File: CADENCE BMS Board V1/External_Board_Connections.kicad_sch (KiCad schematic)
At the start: 42 parts, among them J10 Conn_01x08, J11 Conn_01x06, J12 Conn_01x02, J13 Conn_01x08, J14 Conn_01x04, J15 Conn_01x08, J2 Conn_01x02, J27 USB_C_Receptacle_USB2.0_16P, J3 Conn_01x08, J4 Conn_01x02, J5 Conn_01x01_Socket, J6 Conn_01x01_Socket, J7 Conn_01x01_Socket, J8 Conn_01x01_Socket, J9 Conn_01x04, Q27 Q_PMOS_DGS, Q28 Q_PMOS_DGS, U11 CYPD3177-24LQ

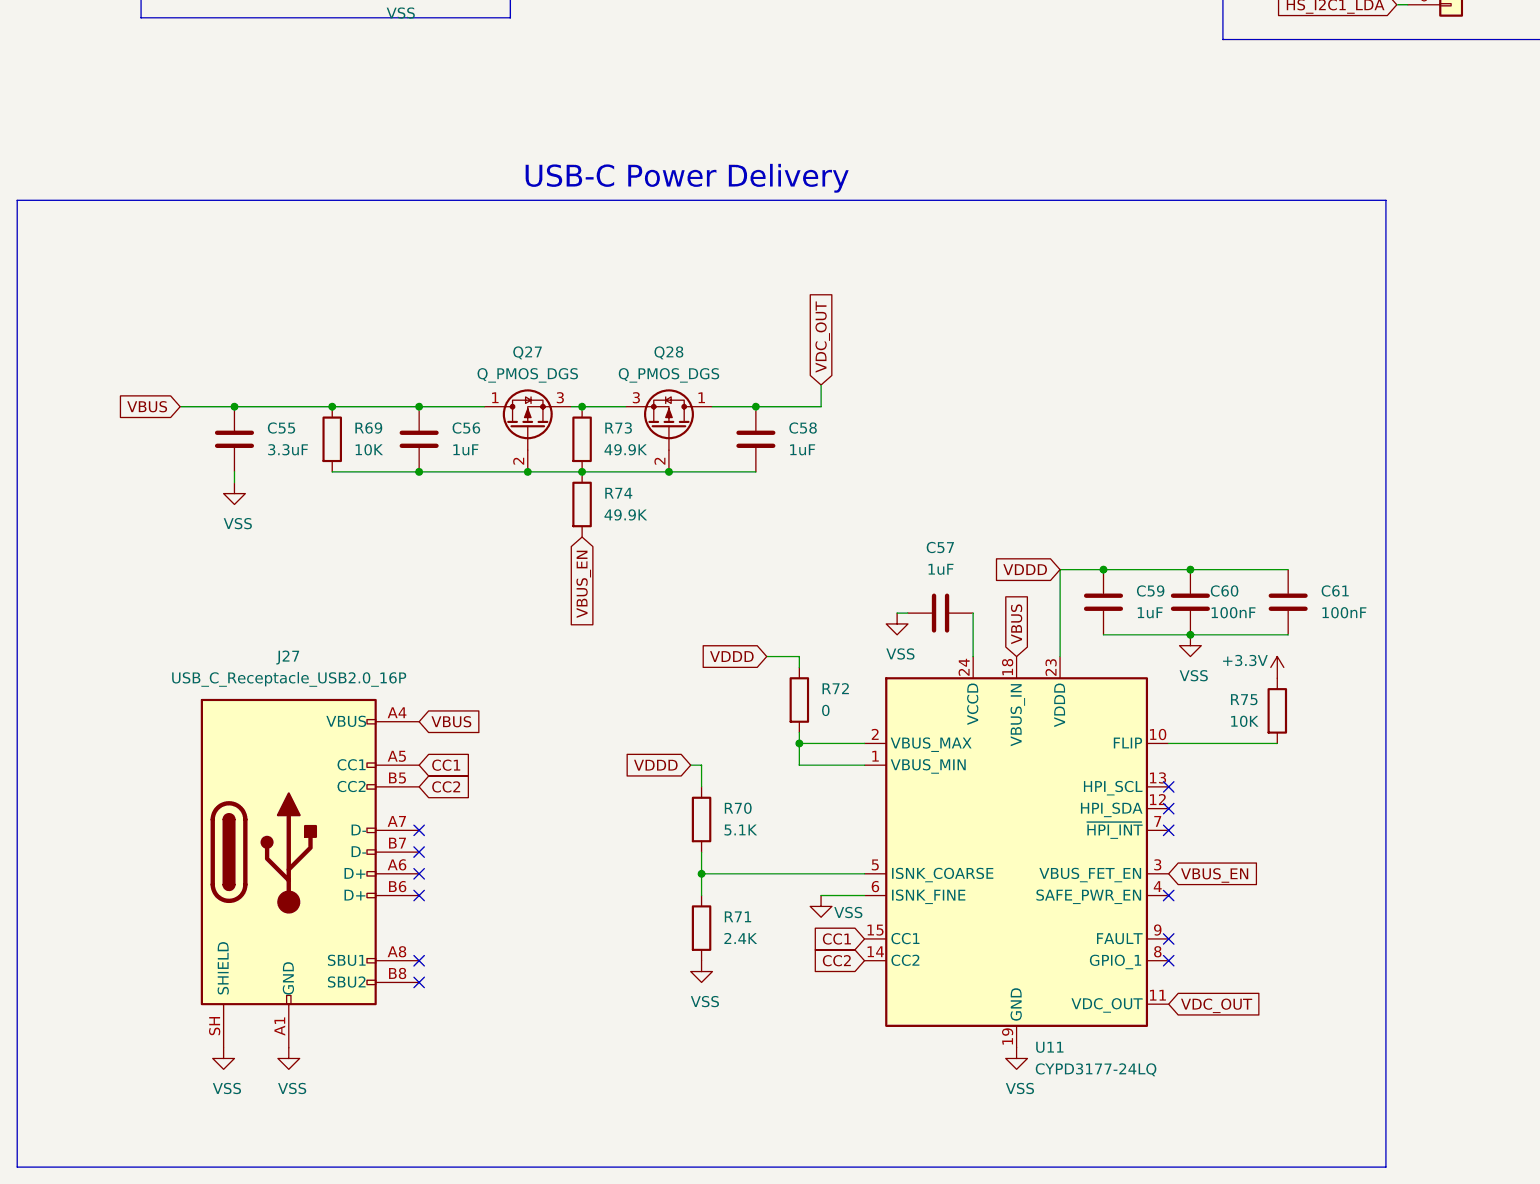
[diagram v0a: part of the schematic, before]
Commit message: Updates for banana plug power testing
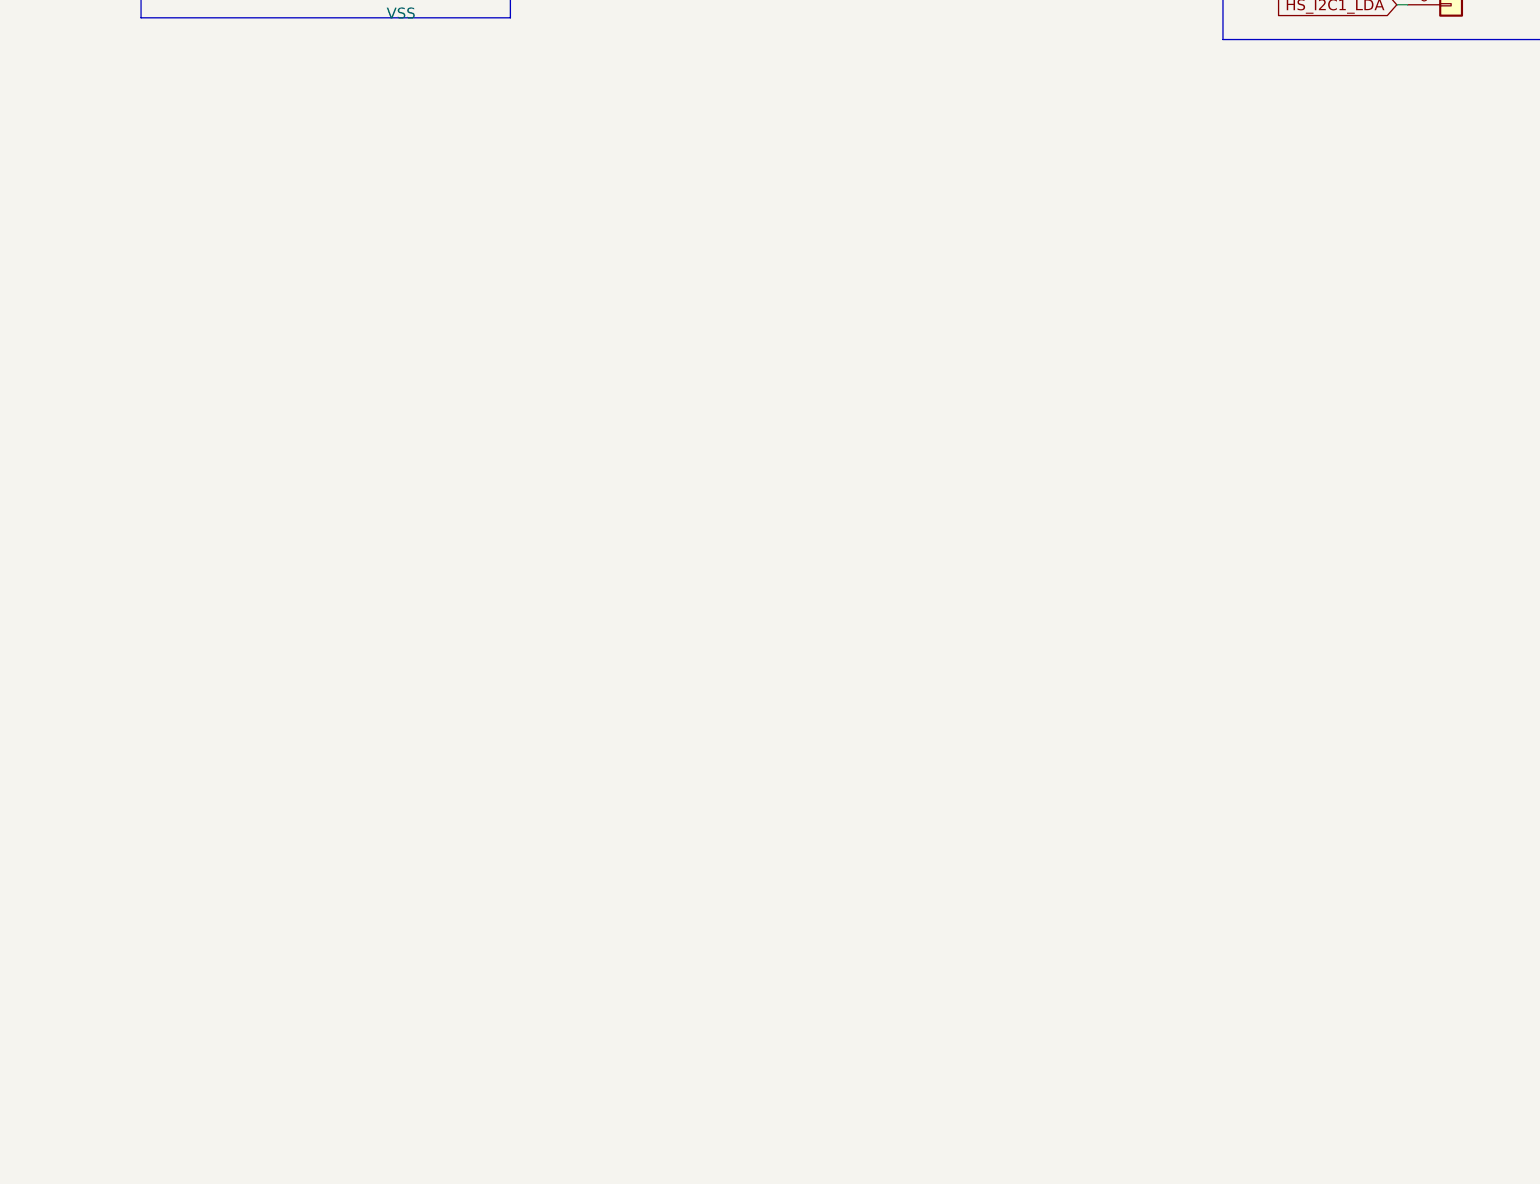
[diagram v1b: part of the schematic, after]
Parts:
- removed C55: 3.3uF, Capacitor_SMD:C_0805_2012Metric, symbol Device:C
- removed C56, C57, C58, C59: 1uF, Capacitor_SMD:C_0805_2012Metric, symbol Device:C
- removed C60, C61: 100nF, Capacitor_SMD:C_0603_1608Metric, symbol Device:C
- removed J27: USB_C_Receptacle_USB2.0_16P, Connector_USB:USB_C_Receptacle_HRO_TYPE-C-31-M-12, symbol Connector:USB_C_Receptacle_USB2.0_16P
- removed Q27, Q28: Q_PMOS_DGS, Package_TO_SOT_SMD:SOT-23, symbol Transistor_FET:Q_PMOS_DGS
- removed R69: 10K, Resistor_SMD:R_0603_1608Metric_Pad0.98x0.95mm_HandSolder, symbol Device:R
- removed R70: 5.1K, Resistor_SMD:R_0603_1608Metric_Pad0.98x0.95mm_HandSolder, symbol Device:R
- removed R71: 2.4K, Resistor_SMD:R_0603_1608Metric, symbol Device:R
- removed R72: 0, Resistor_SMD:R_0603_1608Metric, symbol Device:R
- removed R73, R74: 49.9K, Resistor_SMD:R_0603_1608Metric, symbol Device:R
- removed R75: 10K, Resistor_SMD:R_0603_1608Metric, symbol Device:R
- removed U11: CYPD3177-24LQ, Package_DFN_QFN:QFN-24-1EP_4x4mm_P0.5mm_EP2.75x2.75mm, symbol Interface_USB:CYPD3177-24LQ
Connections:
- no-connect marks 12 -> 0
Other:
- note removed: "USB-C Power Delivery"

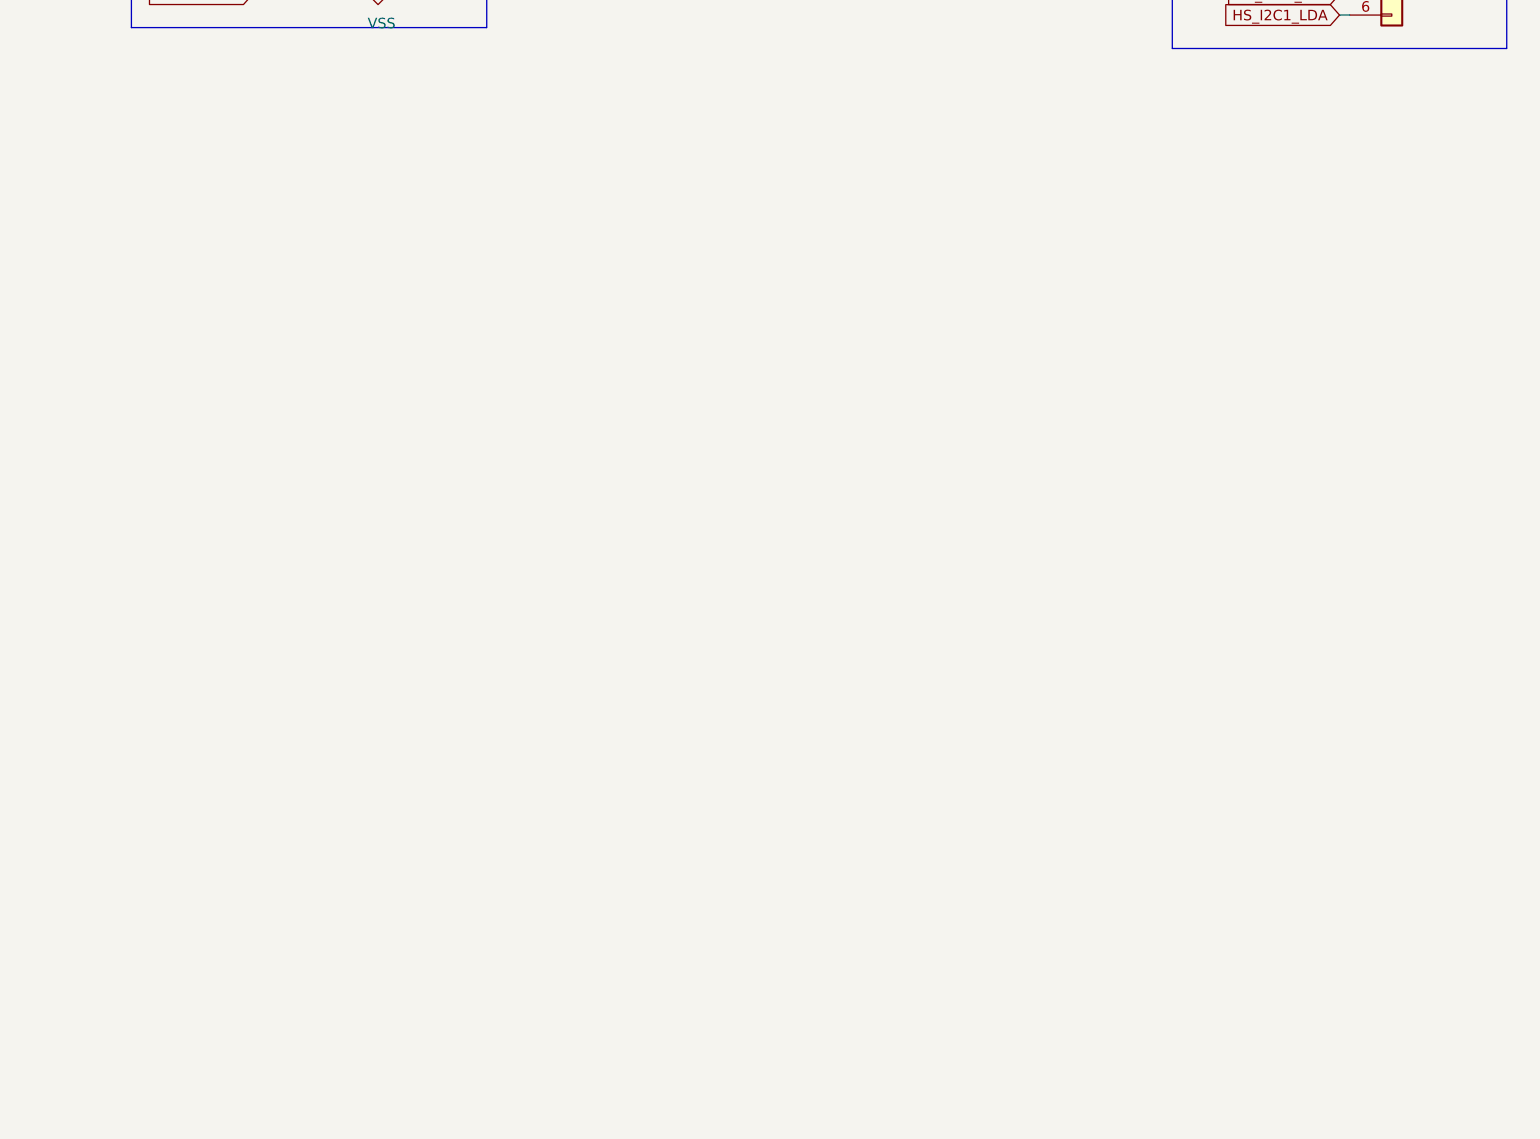
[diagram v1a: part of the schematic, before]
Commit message: Updates for USB-C charging and set up for testing
Revamped USB-C layout to make it cleaner and more compressed and also included schematic parts for adding in Banana plugs for testing the PCB
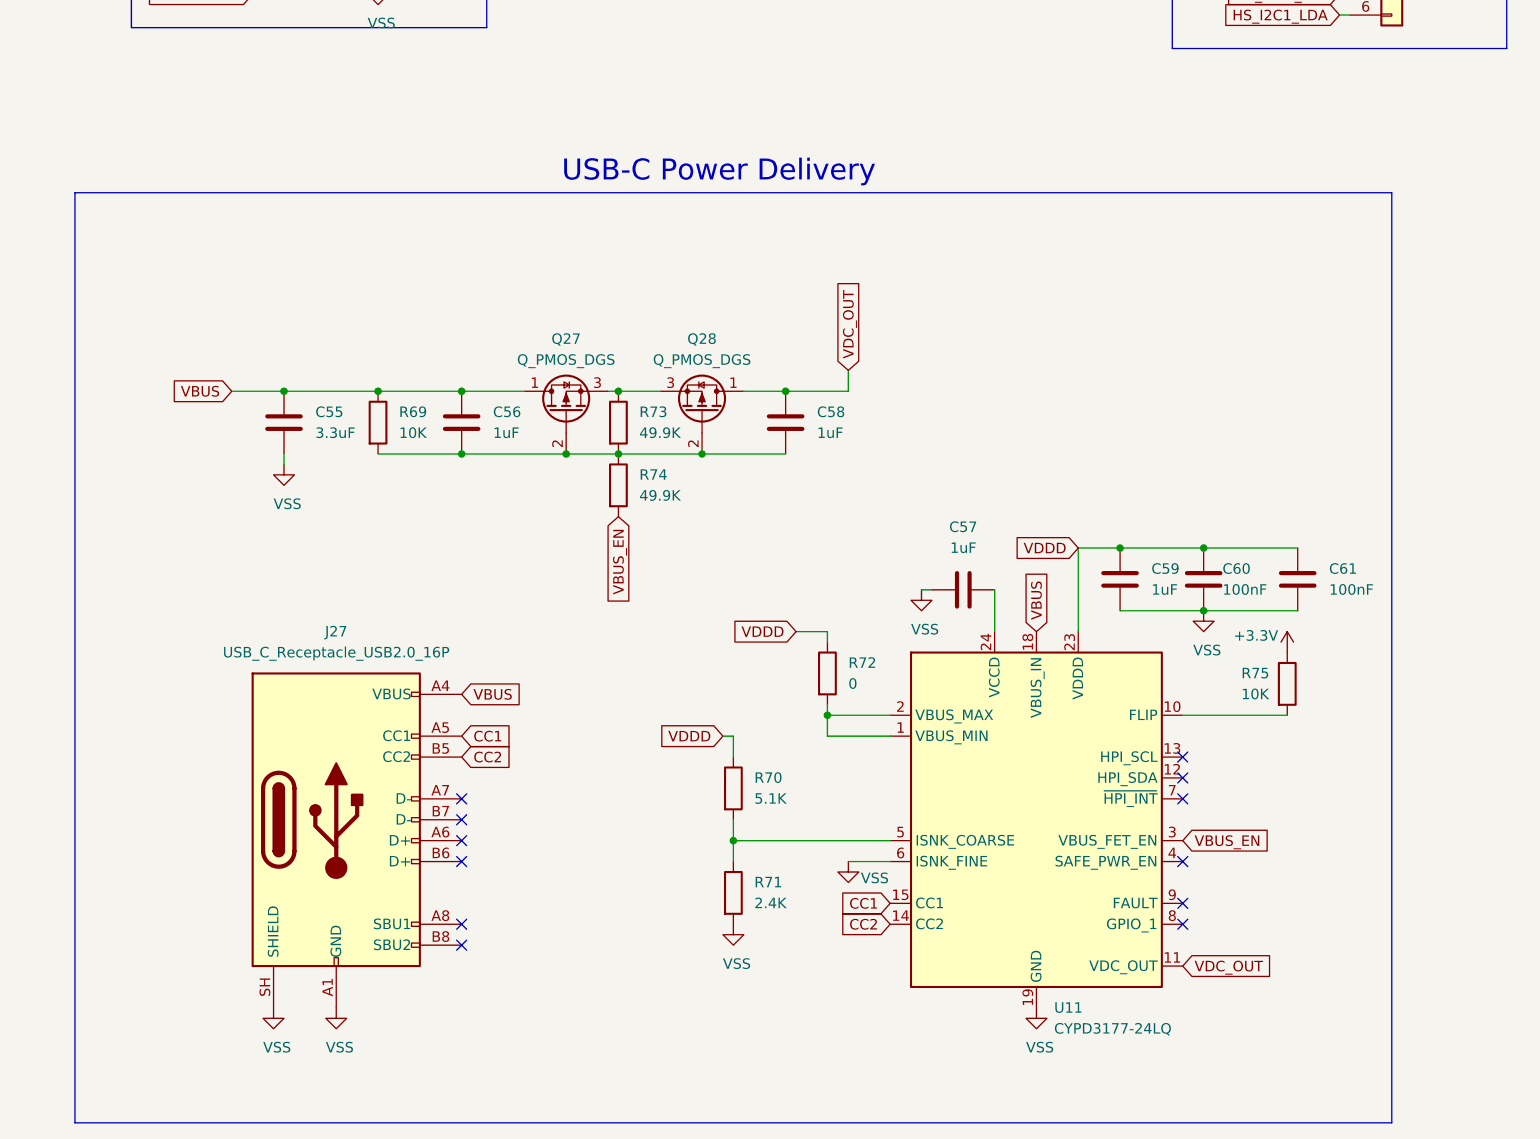
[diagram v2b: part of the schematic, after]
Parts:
- added C55: 3.3uF, Capacitor_SMD:C_0805_2012Metric, symbol Device:C
- added C56, C57, C58, C59: 1uF, Capacitor_SMD:C_0805_2012Metric, symbol Device:C
- added C60, C61: 100nF, Capacitor_SMD:C_0603_1608Metric, symbol Device:C
- added J27: USB_C_Receptacle_USB2.0_16P, Connector_USB:USB_C_Receptacle_HRO_TYPE-C-31-M-12, symbol Connector:USB_C_Receptacle_USB2.0_16P
- added Q27, Q28: Q_PMOS_DGS, Package_TO_SOT_SMD:SOT-23, symbol Transistor_FET:Q_PMOS_DGS
- added R69: 10K, Resistor_SMD:R_0603_1608Metric_Pad0.98x0.95mm_HandSolder, symbol Device:R
- added R70: 5.1K, Resistor_SMD:R_0603_1608Metric_Pad0.98x0.95mm_HandSolder, symbol Device:R
- added R71: 2.4K, Resistor_SMD:R_0603_1608Metric, symbol Device:R
- added R72: 0, Resistor_SMD:R_0603_1608Metric, symbol Device:R
- added R73, R74: 49.9K, Resistor_SMD:R_0603_1608Metric, symbol Device:R
- added R75: 10K, Resistor_SMD:R_0603_1608Metric, symbol Device:R
- added U11: CYPD3177-24LQ, Package_DFN_QFN:QFN-24-1EP_4x4mm_P0.5mm_EP2.75x2.75mm, symbol Interface_USB:CYPD3177-24LQ
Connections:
- net +3.3V: now also R75.1
- net VSS: now also C55.2, C57.1, C59.2, C60.2, C61.2, J27.A1 (GND), J27.A12 (GND), J27.B1 (GND), J27.B12 (GND), J27.SH (SHIELD), R71.2, U11.19 (GND), U11.22 (GND), U11.25 (GND), U11.6 (ISNK_FINE)
- new net: C56.2, C58.2, Q27.2 (G), Q28.2 (G), R69.2, R73.2, R74.1
- new net: R72.2, U11.1 (VBUS_MIN), U11.2 (VBUS_MAX)
- new net: R75.2, U11.10 (FLIP)
- new net: C57.2, U11.24 (VCCD)
- new net: R70.2, R71.1, U11.5 (ISNK_COARSE)
- new net: Q27.3 (S), Q28.3 (S), R73.1
- new net CC1: J27.A5 (CC1), U11.15 (CC1)
- new net CC2: J27.B5 (CC2), U11.14 (CC2)
- new net VBUS: C55.1, C56.1, J27.A4 (VBUS), J27.A9 (VBUS), J27.B4 (VBUS), J27.B9 (VBUS), Q27.1 (D), R69.1, U11.18 (VBUS_IN)
- new net VBUS_EN: R74.2, U11.3 (VBUS_FET_EN)
- new net VDC_OUT: C58.1, Q28.1 (D), U11.11 (VDC_OUT)
- new net VDDD: C59.1, C60.1, C61.1, R70.1, R72.1, U11.23 (VDDD)
- no-connect marks 0 -> 12
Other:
- note added: "USB-C Power Delivery"

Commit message: New connectors and adding in a test setup
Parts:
- added J29, J30: Conn_01x02, Connector_JST:JST_NV_B02P-NV_1x02_P5.00mm_Vertical, symbol Connector_Generic:Conn_01x02
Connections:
- net Cell 1+: no longer J12.1 (Pin_1), J2.1 (Pin_1), J9.1 (Pin_1)
- net VSS: now also J29.2 (Pin_2), J30.2 (Pin_2); no longer J10.5 (Pin_5), J10.6 (Pin_6), J13.5 (Pin_5), J13.6 (Pin_6), J14.4 (Pin_4), J15.5 (Pin_5), J15.6 (Pin_6), J3.5 (Pin_5), J3.6 (Pin_6), TP12.1, TP14.1, TP16.1, TP9.1
- new net Cell 3-: J14.4 (Pin_4)
- new net Solar1-: J10.5 (Pin_5), J10.6 (Pin_6), J13.5 (Pin_5), J13.6 (Pin_6), J15.5 (Pin_5), J15.6 (Pin_6), J3.5 (Pin_5), J3.6 (Pin_6), TP12.1, TP14.1, TP16.1, TP9.1
- new net TEST_PWR: J30.1 (Pin_1)
- new net UNREG: J12.1 (Pin_1), J2.1 (Pin_1), J9.1 (Pin_1)
- new net USB PWR: J29.1 (Pin_1)
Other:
- note added: "2 Amps setup"
- note added: "20 Volts setup"
- note added: "Antenna Board"
- note added: "Chassis is connected with these mounting holes"
- note added: "EBYTE Board"
- note added: "FC Board"
- note added: "Payload Board"
- note added: "Test Connections"
- note removed: "EBYTE board"
- note removed: "FC board"
- note removed: "Payload board"
- moved on the sheet: J12, J2
